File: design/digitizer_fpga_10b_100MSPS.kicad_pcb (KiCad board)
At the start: 4 copper layers, 110 x 60 mm, 281 parts, among them J1 POWER, J2 SWD_01X04, J3 DEBUG_SPI, J4 USB_B_Mini, J5 SMA, J6 JUMPER_DFS/GAIN, J7 DEBUG_FPGA_GPIO, J8 DIGILENT_JTAG_HS2_01X06, SW1 RST, SW2 PROG, U1 LM3880MF-1AA, U10 IS61WV12816EDBLL-10TLI, U11 TLV431ACDBZR, U12 AD9214, U13 XC7S15-FTGB196, U14 IS25LP064A-JKx, U2 NCP59744MN1, U3 NCP59744MN1, U4 NCP59744MN1, U5 NCP59744MN1, U6 STM32H750VBTx, U7 USBLC6-2SC6, U8 FT231XS, U9 ADA4930-1, X1 ASTX-H11-25.000MHZ-T

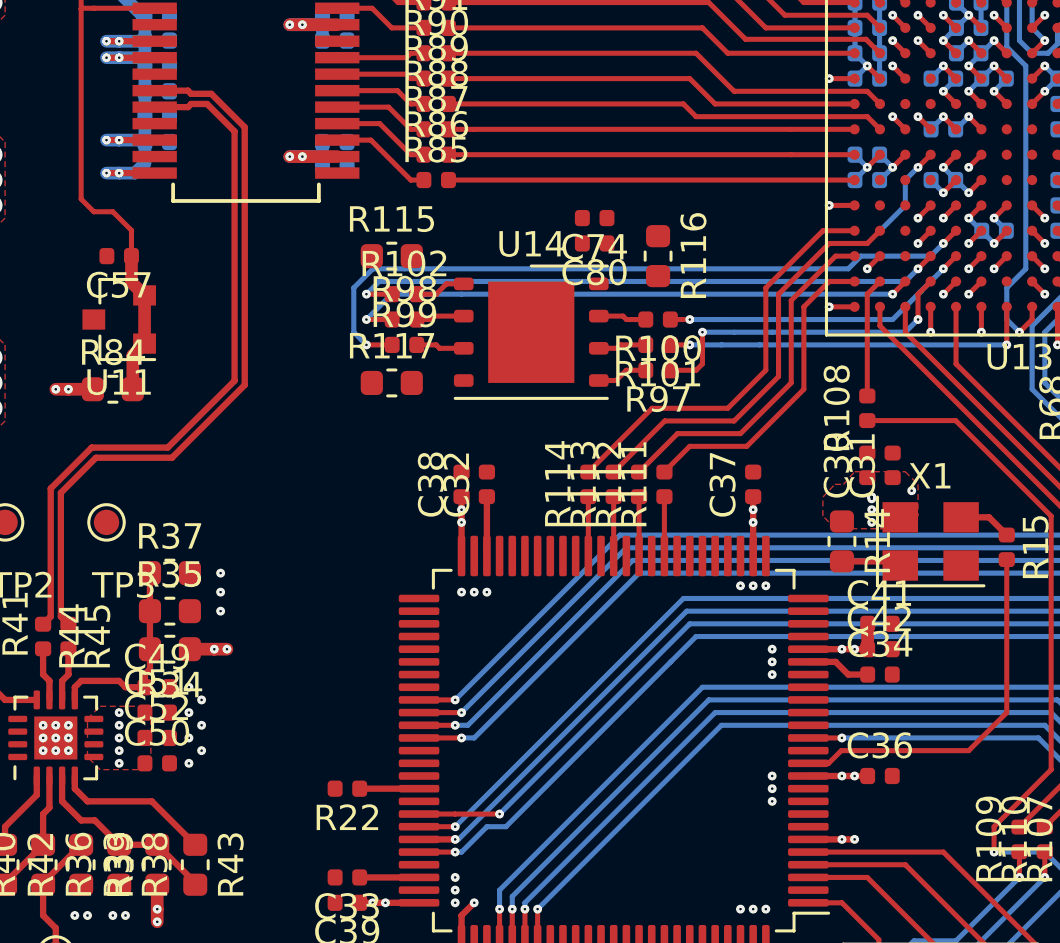
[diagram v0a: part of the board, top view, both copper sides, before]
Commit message: Added clock layout
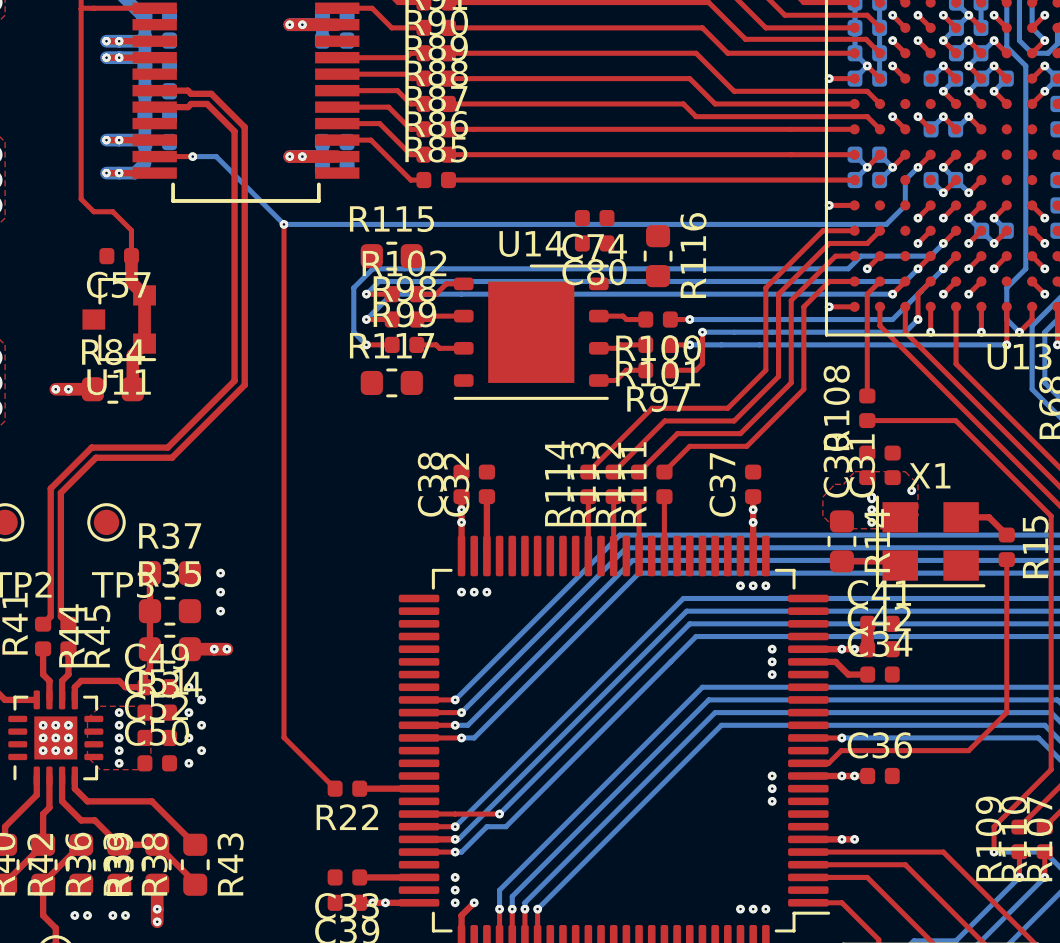
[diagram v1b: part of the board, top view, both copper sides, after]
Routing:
- net /CLK: track 3.83 -> 56.5 mm, vias 1 -> 3
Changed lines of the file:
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@@
     (thickness 1.628)
     (drawings 36)
-    (tracks 1764)
+    (tracks 1772)
     (modules 281)
     (nets 334)
@@
   (gr_line (start 75 90) (end 175 90) (layer "Edge.Cuts") (width 0.05))
   (gr_line (start 70 145) (end 70 95) (layer "Edge.Cuts") (width 0.05))
+  (segment (start 132.75 114.75) (end 133.5 114) (width 0.2) (layer "BOT") (net 46))
+  (segment (start 109 114.75) (end 132.75 114.75) (width 0.2) (layer "BOT") (net 46))
+  (segment (start 111.015 137) (end 109 134.985) (width 0.2) (layer "TOP") (net 46))
+  (segment (start 109 134.985) (end 109 114.75) (width 0.2) (layer "TOP") (net 46))
+  (segment (start 106.325 112.075) (end 109 114.75) (width 0.2) (layer "BOT") (net 46))
+  (segment (start 105.4 112.075) (end 106.325 112.075) (width 0.2) (layer "BOT") (net 46))
+  (via (at 109 114.75) (size 0.35) (drill 0.1) (layers "TOP" "BOT") (net 46))
+  (via (at 105.4 112.075) (size 0.35) (drill 0.1) (layers "TOP" "BOT") (net 46) (status 40000))
+  (segment (start 103.9 112.075) (end 105.4 112.075) (width 0.2) (layer "TOP") (net 46))
   (segment (start 139.75 133) (end 125.5 133) (width 0.2) (layer "BOT") (net 255))
   (segment (start 125.5 133) (end 117.5 141) (width 0.2) (layer "BOT") (net 255))
@@
   (segment (start 134.5 105) (end 134.5 101.485) (width 0.2) (layer "TOP") (net 95))
   (segment (start 135.5 105) (end 135.5 101.485) (width 0.2) (layer "TOP") (net 96))
-  (segment (start 132.5 115) (end 133.5 114) (width 0.2) (layer "BOT") (net 46))
   (segment (start 133.5 114) (end 133.5 113) (width 0.2) (layer "BOT") (net 46))
   (segment (start 133.5 113) (end 134 112.5) (width 0.2) (layer "BOT") (net 46))

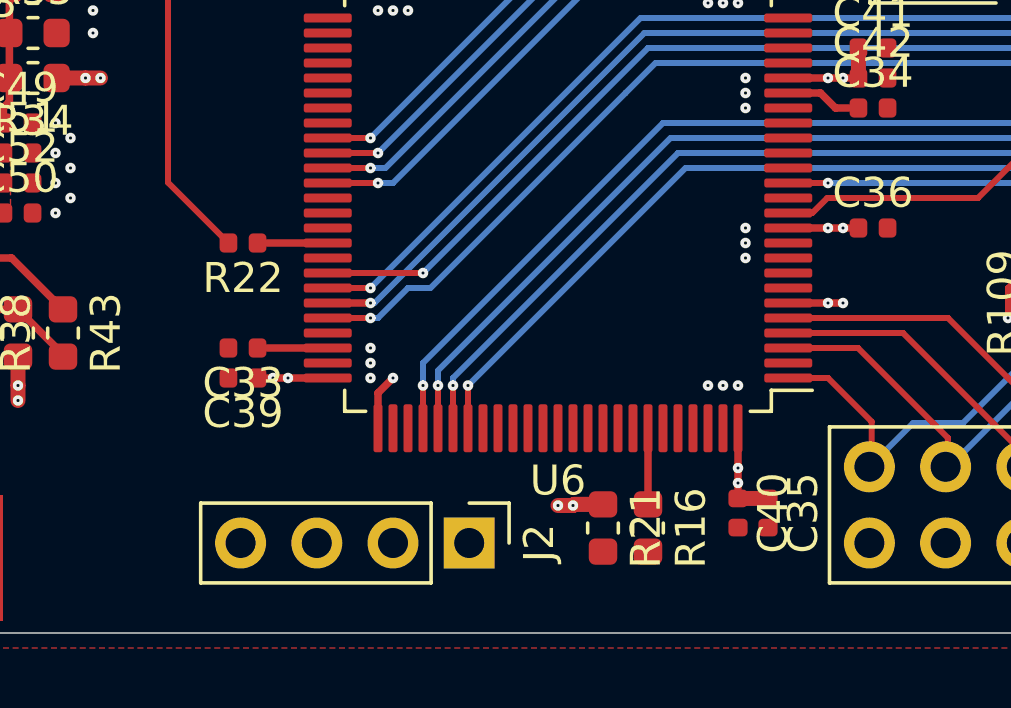
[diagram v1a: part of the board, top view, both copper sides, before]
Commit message: Added SWD layout
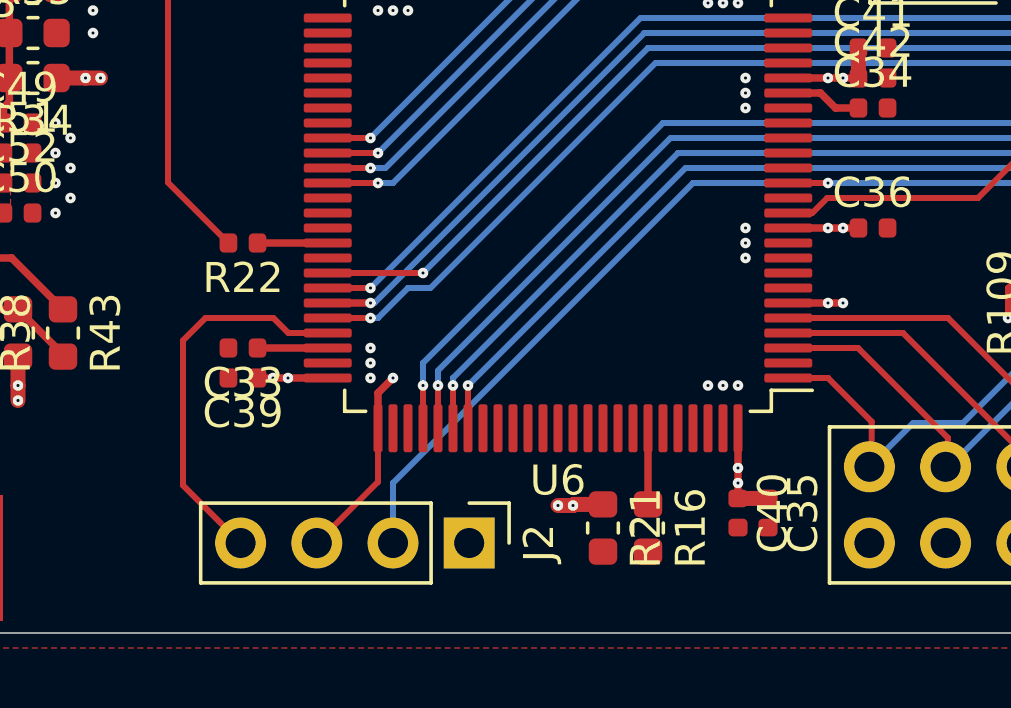
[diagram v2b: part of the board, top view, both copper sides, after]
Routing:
- net /~RST: track 21.1 -> 41.8 mm
- net /MCU/SWDIO: track 0.00 -> 12.9 mm
- net /MCU/SWCLK: track 1.88 -> 6.55 mm
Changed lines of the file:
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@@
     (thickness 1.628)
     (drawings 36)
-    (tracks 1772)
+    (tracks 1783)
     (modules 281)
     (nets 334)
@@
   (gr_line (start 75 90) (end 175 90) (layer "Edge.Cuts") (width 0.05))
   (gr_line (start 70 145) (end 70 95) (layer "Edge.Cuts") (width 0.05))
+  (segment (start 131 135) (end 126.5 135) (width 0.2) (layer "BOT") (net 10))
+  (segment (start 126.5 135) (end 116.5 145) (width 0.2) (layer "BOT") (net 10))
+  (segment (start 116.5 145) (end 116.5 147) (width 0.2) (layer "BOT") (net 10))
+  (segment (start 113.0125 140) (end 112.5125 139.5) (width 0.2) (layer "TOP") (net 18))
+  (segment (start 114.325 140) (end 113.0125 140) (width 0.2) (layer "TOP") (net 18))
+  (segment (start 112.5125 139.5) (end 110.25 139.5) (width 0.2) (layer "TOP") (net 18))
+  (segment (start 110.25 139.5) (end 109.5 140.25) (width 0.2) (layer "TOP") (net 18))
+  (segment (start 109.5 140.25) (end 109.5 145.08) (width 0.2) (layer "TOP") (net 18))
+  (segment (start 109.5 145.08) (end 111.42 147) (width 0.2) (layer "TOP") (net 18))
+  (segment (start 116 143.175) (end 116 144.96) (width 0.2) (layer "TOP") (net 19))
+  (segment (start 116 144.96) (end 113.96 147) (width 0.2) (layer "TOP") (net 19))
   (segment (start 132.75 114.75) (end 133.5 114) (width 0.2) (layer "BOT") (net 46))
   (segment (start 109 114.75) (end 132.75 114.75) (width 0.2) (layer "BOT") (net 46))

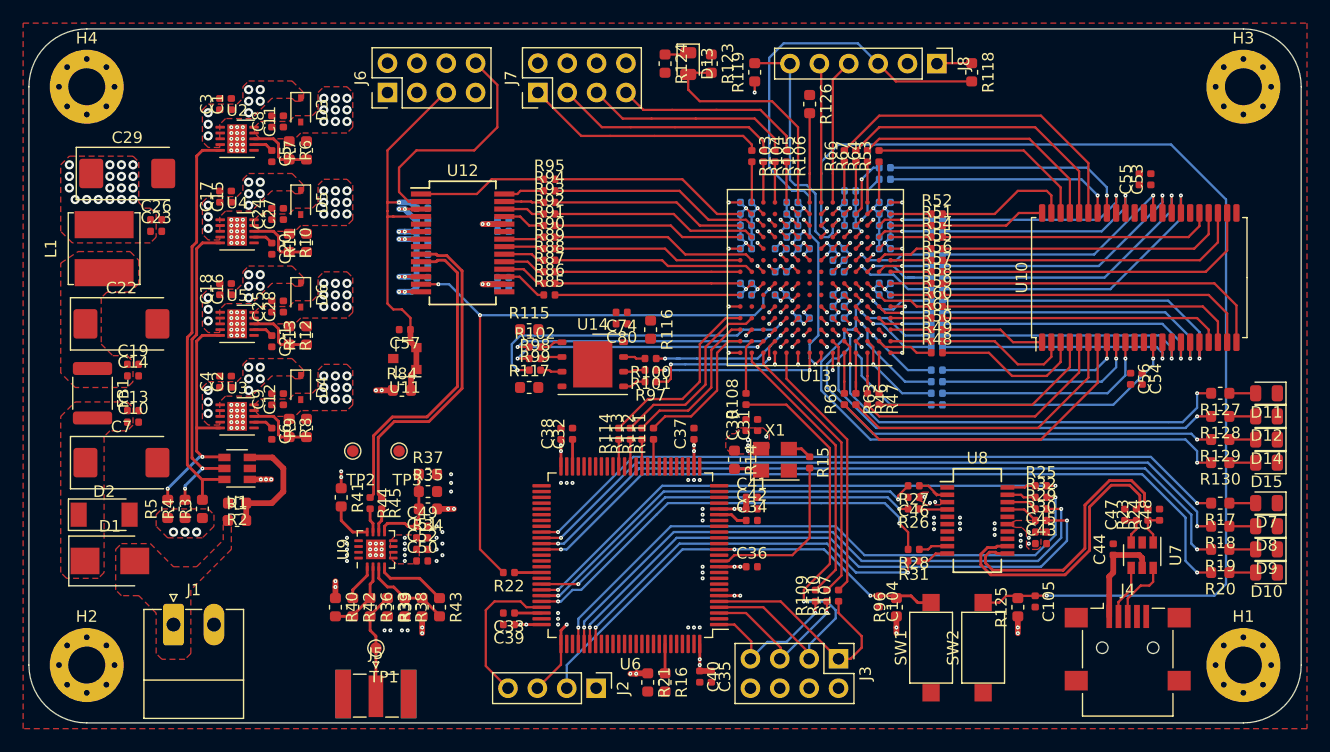
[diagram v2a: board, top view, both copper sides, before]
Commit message: Added some power layout
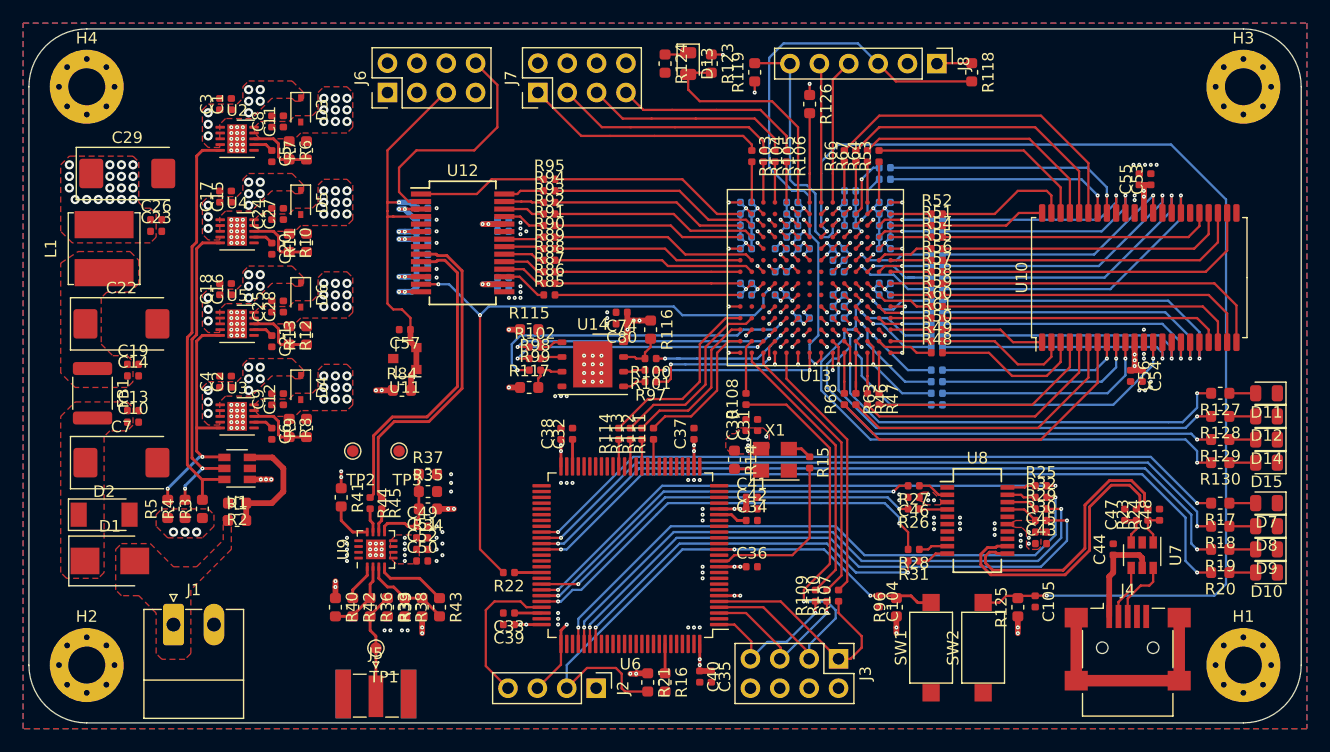
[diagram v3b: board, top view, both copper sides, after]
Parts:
- moved C54 0.25 mm to (166.2, 120.0)
- moved C56 0.25 mm to (165.2, 120.0)
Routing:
- net Net-(J4-Pad6): track 0.00 -> 19.8 mm
- net +3V3D: track 60.1 -> 75.7 mm, vias 56 -> 66
- net /~RST: track 41.8 -> 51.1 mm
- net Net-(R100-Pad2): track 1.91 -> 3.82 mm
- net Net-(R117-Pad2): track 1.91 -> 3.49 mm
- net Net-(R102-Pad2): track 2.02 -> 3.60 mm
- net /~FTDI_RTS: track 36.4 -> 35.6 mm
- net /CLK: track 56.5 -> 57.1 mm
- net GND: vias 173 -> 222
- added copper zone on B.Cu, net GND
